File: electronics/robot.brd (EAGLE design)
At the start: 170.3 x 155.9 mm, 92 parts, among them J1 USB-B, J3 B6B-ZR, J4 B6B-ZR, J5 B6B-ZR, J6 KICKER, Q1 IRLMS2002TRPBF, Q2 IRLMS2002TRPBF, Q3 NPN_BC817,215, Q4 SUD50N04-8M8P-4GE3, Q5 NPN_BC817,215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

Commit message: Electronics rework wip
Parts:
- R18: value 56K -> 68K
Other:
- board text added: "Robot Soccer Kit rev2"
- board text removed: "Robot Soccer Kit rev0"
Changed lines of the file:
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@@
 <circle x="10.176328125" y="33.034390625" radius="3.83270625" width="0" layer="41"/>
 <circle x="10.150928125" y="33.034390625" radius="3.777859375" width="0" layer="42"/>
-<text x="-45.728025" y="-58.419196875" size="1.778" layer="25" rot="R120">Robot Soccer Kit rev0</text>
+<text x="-45.728025" y="-58.419196875" size="1.778" layer="25" rot="R120">Robot Soccer Kit rev2</text>
 <rectangle x1="-13.462" y1="15.386" x2="13.538" y2="40.386" layer="51" rot="R180"/>
 <rectangle x1="-37.796334375" y1="-26.39840625" x2="-10.796334375" y2="-1.39840625" layer="51" rot="R300"/>
@@
 <attribute name="FARNELL" value="2577180RL" x="24.4348" y="10.2616" size="1.778" layer="27" rot="R180" display="off"/>
 </element>
-<element name="R18" library="SparkFun-Resistors" package="0805" value="56K" x="22.7076" y="14.6812">
+<element name="R18" library="SparkFun-Resistors" package="0805" value="68K" x="22.7076" y="14.6812">
 <attribute name="FARNELL" value="2074486" x="22.7076" y="14.6812" size="1.778" layer="27" display="off"/>
 <attribute name="PROD_ID" value="RES-11622" x="22.7076" y="14.6812" size="1.778" layer="27" display="off"/>

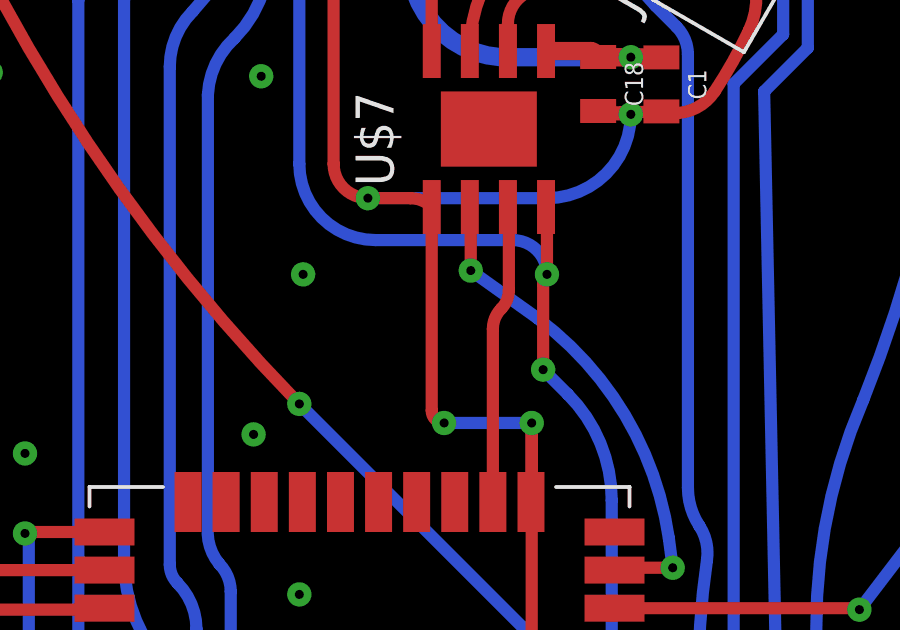
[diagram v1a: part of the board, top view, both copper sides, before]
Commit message: Adding 5k pulling resistor between M1A and M1B
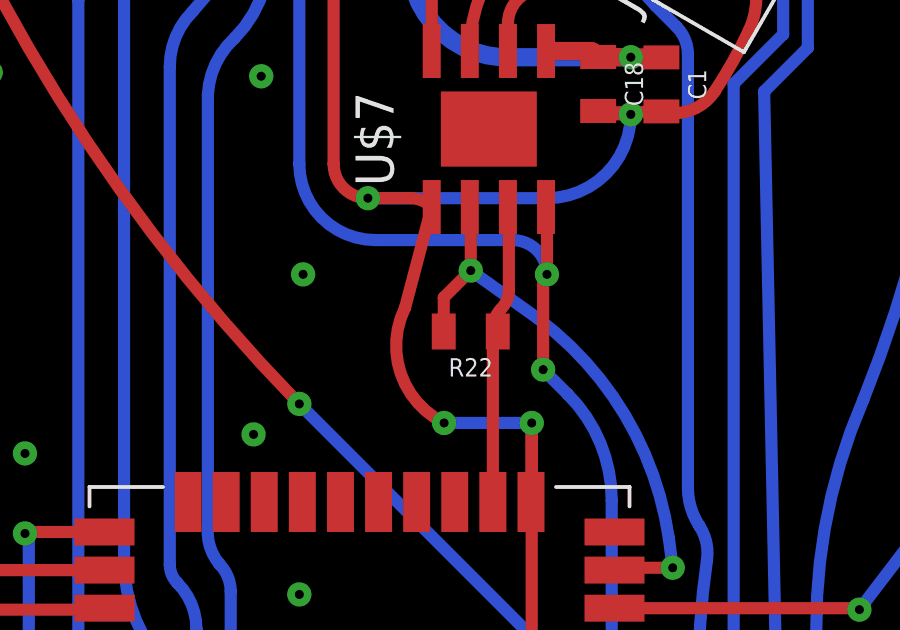
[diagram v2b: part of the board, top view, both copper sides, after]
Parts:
- added R22: 5K, SparkFun-Resistors:0805
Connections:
- net M1A: now also R22.1
- net M1B: now also R22.2
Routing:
- net M1B: track 16.3 -> 18.7 mm
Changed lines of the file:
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@@
 <attribute name="VALUE" value="0.33µF" x="-44.66480625" y="4.181571875" size="1.778" layer="27" rot="R120" display="off"/>
+</element>
+<element name="R22" library="SparkFun-Resistors" package="0805" value="5K" x="3.556" y="-17.018" rot="R180">
+<attribute name="FARNELL" value="2446926" x="3.175" y="-17.018" size="1.778" layer="27" rot="R180" display="off"/>
+<attribute name="PROD_ID" value="RES-11622" x="3.175" y="-17.018" size="1.778" layer="27" rot="R180" display="off"/>
+<attribute name="VALUE" value="0.3" x="3.175" y="-17.018" size="1.778" layer="27" rot="R180" display="off"/>
 </element>
 </elements>
@@
 <wire x1="5.588" y1="-20.066" x2="2.667" y2="-20.066" width="0.4064" layer="16"/>
 <via x="2.667" y="-20.066" extent="1-16" drill="0.3" diameter="0.8128" shape="octagon"/>
-<wire x1="2.667" y1="-20.066" x2="2.254615625" y2="-19.653615625" width="0.4064" layer="1" curve="-90"/>
-<wire x1="2.254615625" y1="-19.653615625" x2="2.254615625" y2="-12.86823125" width="0.4064" layer="1"/>
+<wire x1="2.667" y1="-20.066" x2="1.365615625" y2="-16.224615625" width="0.4064" layer="1" curve="-90"/>
+<wire x1="1.365615625" y1="-16.224615625" x2="2.254615625" y2="-12.86823125" width="0.4064" layer="1"/>
 <wire x1="-1.016" y1="-4.064" x2="-1.016" y2="-11.43" width="0.4064" layer="1"/>
 <wire x1="-1.016" y1="-11.43" x2="0.127" y2="-12.573" width="0.4064" layer="1" curve="90"/>
@@
 <wire x1="4.826" y1="-15.642790625" x2="4.826" y2="-12.944" width="0.4064" layer="1"/>
 <wire x1="4.794615625" y1="-12.86823125" x2="4.826" y2="-12.944" width="0.4064" layer="1" curve="-45"/>
+<contactref element="R22" pad="1"/>
+<wire x1="4.2926" y1="-16.93053125" x2="4.36853125" y2="-16.93053125" width="0.4064" layer="1"/>
+<wire x1="4.36853125" y1="-16.93053125" x2="4.456" y2="-17.018" width="0.4064" layer="1"/>
 </signal>
 <signal name="M1B">
@@
 <wire x1="8.3476" y1="-24.9704" x2="8.536875" y2="-24.892" width="0.4064" layer="1" curve="-45"/>
 <wire x1="8.536875" y1="-24.892" x2="10.287" y2="-24.892" width="0.4064" layer="1"/>
+<contactref element="R22" pad="2"/>
+<wire x1="2.656" y1="-17.018" x2="2.656" y2="-15.886" width="0.4064" layer="1"/>
+<wire x1="2.656" y1="-15.886" x2="3.556" y2="-14.986" width="0.4064" layer="1"/>
 </signal>
 <signal name="M2P2" class="1">
